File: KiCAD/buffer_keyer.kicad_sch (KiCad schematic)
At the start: 56 parts, among them J1 Conn_01x02_Pin, J2 Conn_01x02_Pin, J3 Conn_01x02_Pin, T1 2N3906, T2 2N3906, U3 MC1496, U4 MCP4921, U6 LM7171xIN, U7 LM7171xIN, U8 MCP4728

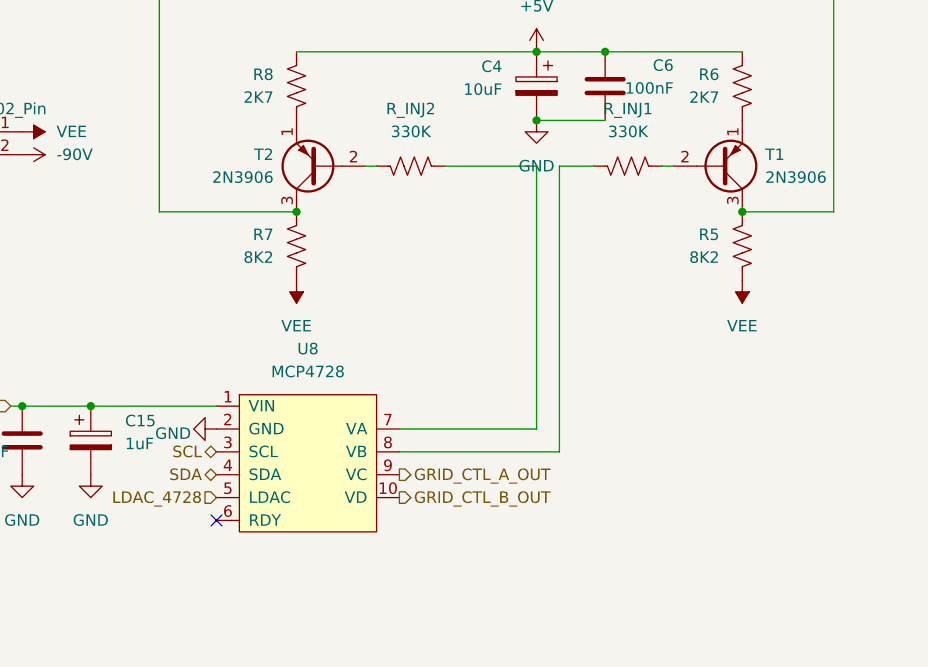
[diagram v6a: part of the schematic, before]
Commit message: kicad: fill missing footprints across active sheets + MCP4728 breakout footprint
Footprint sweep across the analog control board sheets. All active sheets
now clean except U2 (Metro), which is intentionally off-PCB per the
Wingshield-plus-jumpers connection strategy.

Auto-assigned via tools/assign_cap_footprints.py:
  - buffer_keyer: C39, C40 (100 nF, THT disc D5.0mm P5.00mm) -- the null-
    trim bypass caps at R_INJ1 / R_INJ2 that ground the DAC output side
    of the 330K injection resistors going into T1 and T2
  - arduino: C36, C38 (100 nF THT disc), C37 (10 uF radial electrolytic)
  - interface: C34 (100 nF), C35 (10 uF)

Manual assignments:
  - interface: R26, R27, R28, R29 -> R_Axial_DIN0207_L6.3mm axial THT
    (matching the other 1/4W metal-film resistors used throughout)
  - interface: J4 (RJ45 socket) -> xmitter:Amphenol_RJE1D-188_Horizontal_Shielded
  - arduino: J6, J7, J8, J9, J10 -> PinHeader_1x02_P2.54mm_Vertical
  - buffer_keyer: U8 (MCP4728 breakout) -> new custom footprint

New custom footprint xmitter:Adafruit_MCP4728_Breakout:
  - Board 1.00 x 0.70 in (25.4 x 17.78 mm)
  - Four NPTH 2.5 mm mounting holes on 0.80 x 0.50 in spacing
  - 10 THT pads in two rows of 5, pad numbers match the xmitter:MCP4728
    symbol (1=VIN, 2=GND, 3=SCL, 4=SDA, 5=LDAC, 6=RDY, 7=VA, 8=VB, 9=VC,
    10=VD)
  - Pins 3 (SCL) and 4 (SDA) will be left unrouted on the parent PCB
    per the STEMMA QT daisy-chain topology decision -- I2C reaches the
    MCP4728 via a STEMMA cable from the Si5351 breakout, not via PCB
    traces
  - descr field flags "VERIFY silk-label to pad-number correspondence
    against the physical breakout before routing" -- Adafruit revisions
    vary and the specific row assignment was inferred from the
    datasheet fab print on page 20 plus the symbol pin numbering

Also committing Documentation/Components/MCP4728_datasheet.pdf and
Documentation/Components/cd4050b.pdf datasheets that were sitting
uncommitted.

Co-Authored-By: Claude Opus 4.7 <nor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
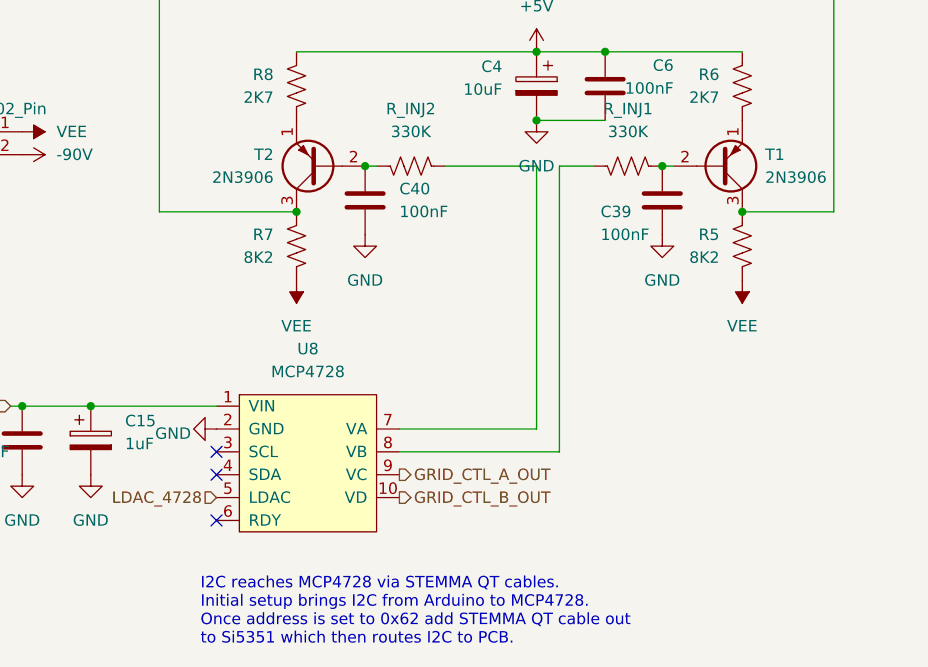
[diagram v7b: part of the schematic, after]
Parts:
- added C39, C40: 100nF, Capacitor_THT:C_Disc_D5.0mm_W2.5mm_P5.00mm, symbol Device:C
- U8: footprint (none) -> xmitter:Adafruit_MCP4728_Breakout
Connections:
- net GND: now also C39.2, C40.2
- net at R_INJ2.2, T2.2 (B): now also C40.1
- net at R_INJ1.1, T1.2 (B): now also C39.1
- net SCL: no longer names the net of U8.3 (SCL)
- net SDA: no longer names the net of U8.4 (SDA)
- no-connect marks 5 -> 7
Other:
- note added: "I2C reaches MCP4728 via STEMMA QT cables. Initial setup brings I2C from Arduino to MCP4728. Once address is set to 0x62 add STEMMA QT cable out to Si5351 which then routes I2C to PCB."

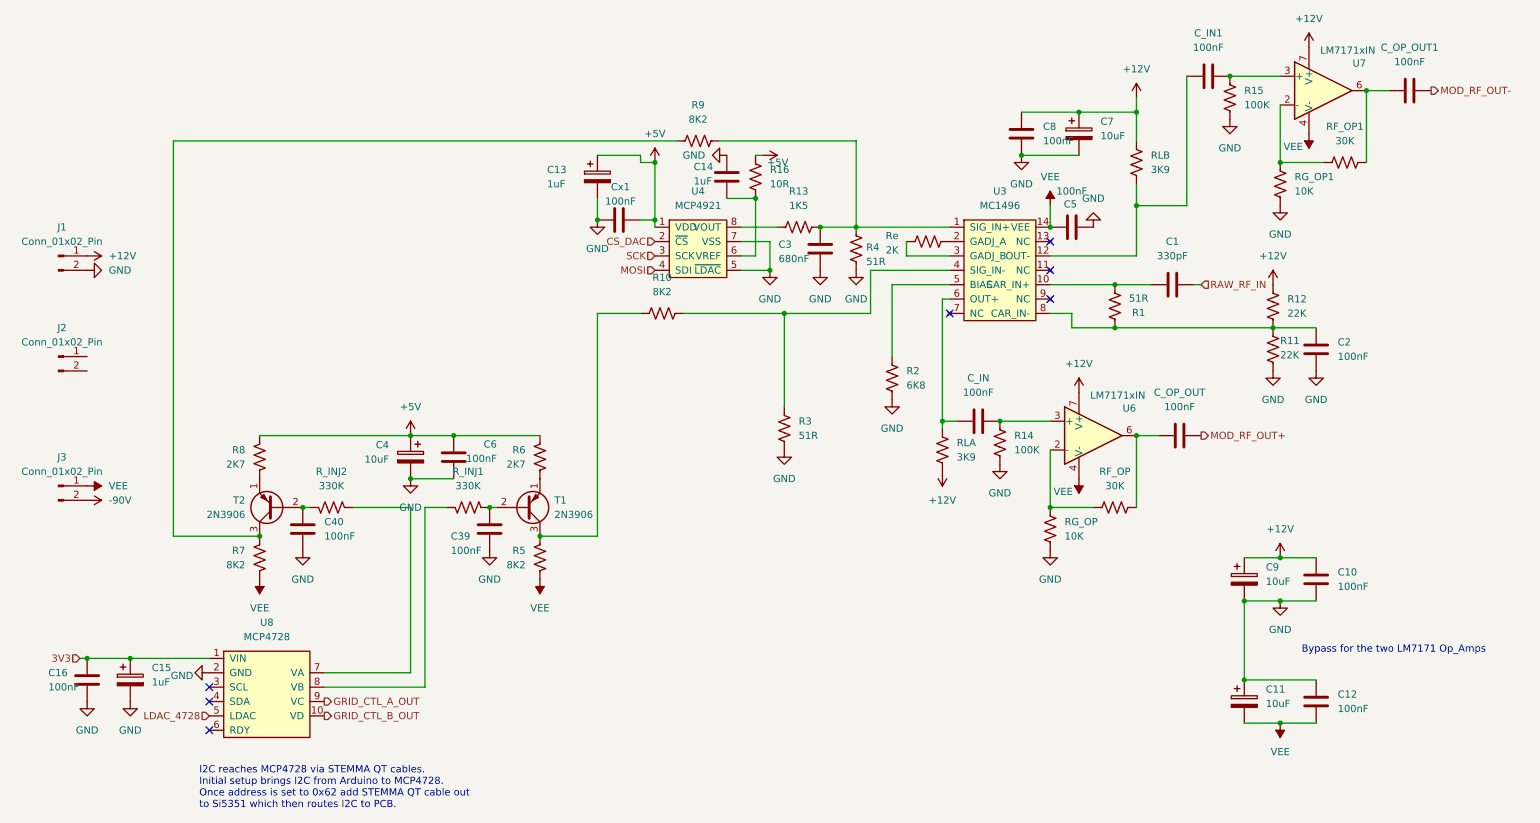
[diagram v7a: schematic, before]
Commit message: schematic: I2C topology flip + CD14538B heartbeat + pre-layout audit
- Documentation updates for the STEMMA-QT topology flip (MCP4728 upstream
  of Si5351): design_review_7-5-26 C1 marked resolved, build_checklist
  Phase 1 gets the 6-step first-boot procedure, cw_envelope_keyer I2C
  address section rewritten, front_panel_interface signal-chain diagram
  refreshed.
- CD14538B dual retriggerable monostable added to xmitter.kicad_sym
  (PDIP-16, pinout verified against datasheet fig. 1), plus datasheet
  file.
- Arduino sheet: CD14538B heartbeat topology on Q5 HV contactor -- U18
  + R30 470K + C41 1uF timing (t_w ~470 ms), Q7 series FET stack,
  C42/C43 VDD bypass and bulk.
- Pre-layout audit output as Documentation/punch_list_7-6-26.txt (list
  of blockers before PCB layout, ordered by severity).

Co-Authored-By: Claude Opus 4.7 (1M context) <noreply@anthropic.com>
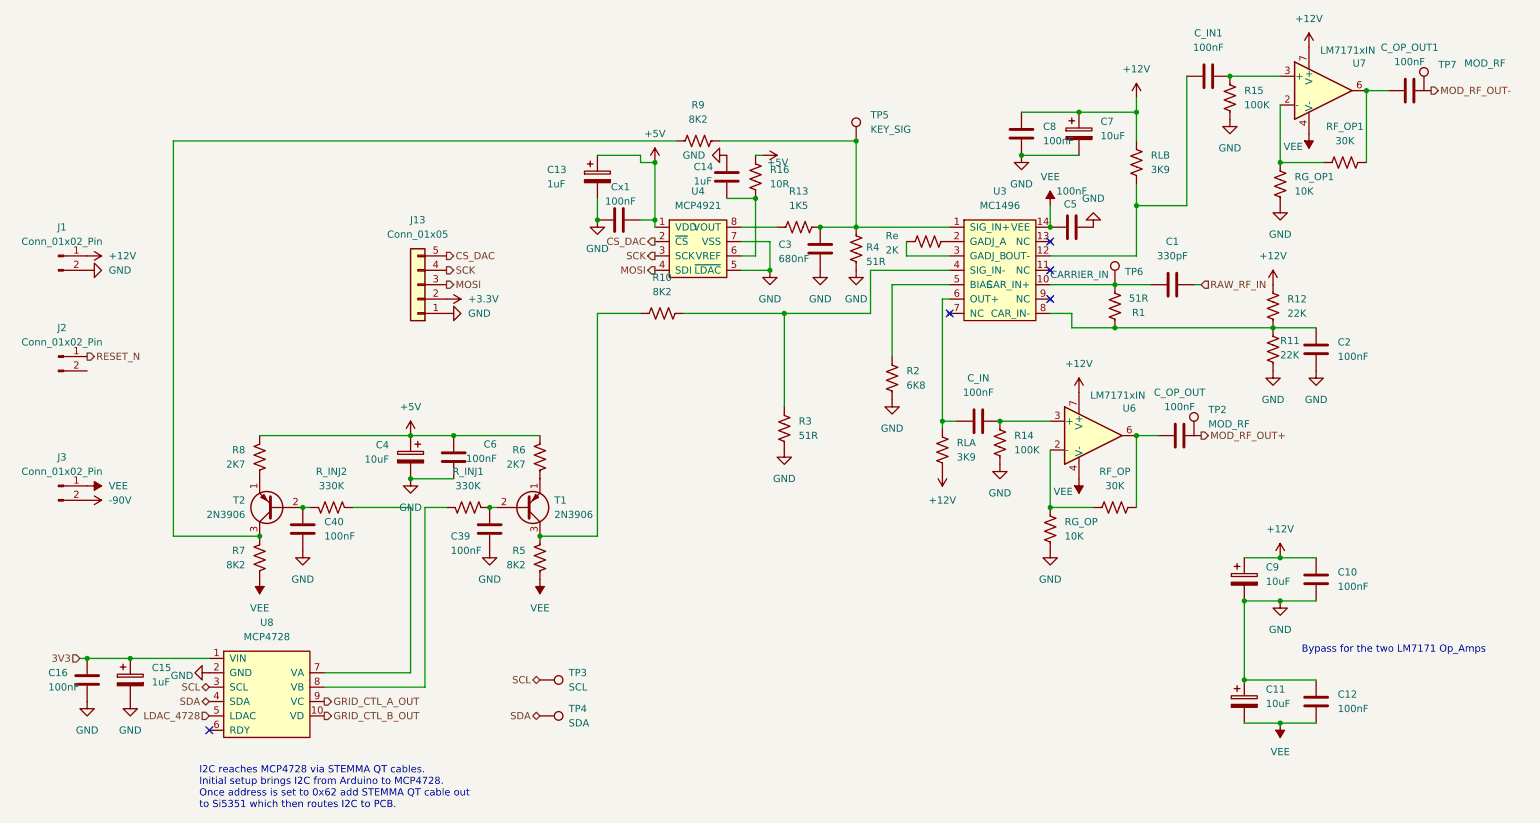
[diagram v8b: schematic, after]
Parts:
- added J13: Conn_01x05, symbol Connector_Generic:Conn_01x05
- added TP2, TP7: MOD_RF, Connector_PinHeader_2.54mm:PinHeader_1x01_P2.54mm_Vertical, symbol xmitter:xTP
- added TP3: SCL, Connector_PinHeader_2.54mm:PinHeader_1x01_P2.54mm_Vertical, symbol xmitter:xTP
- added TP4: SDA, Connector_PinHeader_2.54mm:PinHeader_1x01_P2.54mm_Vertical, symbol xmitter:xTP
- added TP5: KEY_SIG, Connector_PinHeader_2.54mm:PinHeader_1x01_P2.54mm_Vertical, symbol xmitter:xTP
- added TP6: CARRIER_IN, Connector_PinHeader_2.54mm:PinHeader_1x01_P2.54mm_Vertical, symbol xmitter:xTP
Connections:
- net CS_DAC: now also J13.5 (Pin_5)
- net GND: now also J13.1 (Pin_1)
- net MOSI: now also J13.3 (Pin_3)
- net SCK: now also J13.4 (Pin_4)
- net at C3.1, R13.2, R4.1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: now also TP5.1
- net at C1.1, R1.2, U3.10 (CAR_IN+): now also TP6.1
- net SCL: now reaches U8.3 (SCL)
- net SCL: now also TP3.1
- net SDA: now reaches U8.4 (SDA)
- net SDA: now also TP4.1
- net RESET_N: now reaches J2.1 (Pin_1)
- new net +3.3V: J13.2 (Pin_2)
- no-connect marks 7 -> 5
